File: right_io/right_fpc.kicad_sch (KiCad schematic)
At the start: 1 part

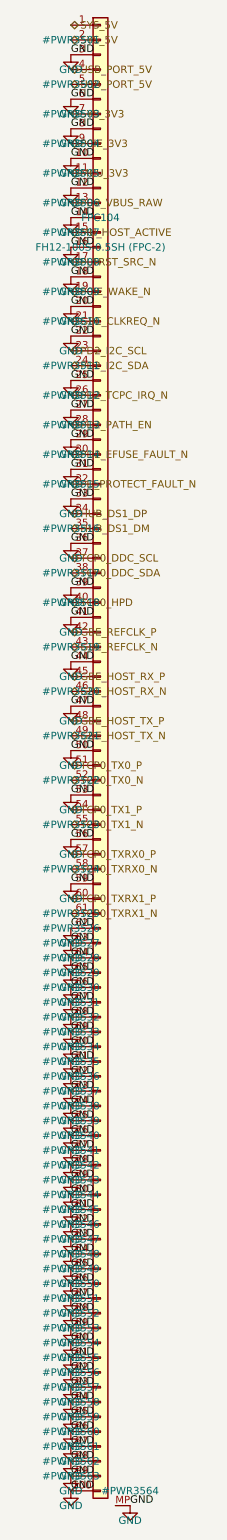
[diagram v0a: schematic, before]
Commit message: Phase 4 deep audit: FH41-68S connectors, placement hygiene, one-shot fixes
Found and fixed four board-killers in the pre-fab audit:

1. Fictional connector: the Hirose FH12 series stops at 60 positions, so
   the 100-pin FH12-100S used for FPC-1/FPC-2 does not exist.  Replaced
   with the FH41-68S-0.5SH(05) (shielded-FFC, 68 positions; FPC-1 uses
   pins 1-53, FPC-2 pins 1-61):
   - new footprint derived from KiCad's FH41-30S (68 signal pads, MP at
     +/-18, 14 SH solder-holds, 38mm body) with SH pads tied to GND
   - new 68-pin symbol (Conn_01x68_FFC_MP), pin maps trimmed to 68
   - fictional FH12-100S footprint/symbol/script removed
   - cable spec updated (68-pin shielded FFC, one type for both)

2. Connector courtyard conflicts: parts sat under connector bodies
   (pads cleared, bodies collided).  Placement now enforces courtyard
   clearance against the connector body; the resolver scans with
   courtyard checks; a double-shift bug that hid re-placed parts' true
   positions was fixed.

3. FPC-3 orientation: the FH12's FPC enters from the +y side; both FPC-3
   connectors faced away from the seam.  FPC105 -> (123.5, 6.5) rot 180,
   FPC106 -> (30, 54) rot 0 so the cable exits the center bottom edge
   and enters the BMS top edge.

4. Original-layout defects: 16 genuine pad-pad shorts (inductor pads
   swallowing caps, passives on each other, parts on mounting holes) and
   23 parts inside the hinge cutouts (physically off the board) are all
   moved to legal spots; zones refilled against the final placement.

New post-build hygiene sweep (fix_board_hygiene.py) uses the final board
text as the geometry oracle, converges to a clean state, and reports
residuals instead of dropping them.

Final DRC: 0 shorts / 0 clearance / 0 hole violations on all four boards
(bms fully clean).  Remaining: courtyard touches around the Mu socket and
M.2 slot (design-inherent moat), chassis-edge copper, zone islands, silk
cosmetics, and unrouted nets (Phase 4b).  Gate: SCHEMATIC R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
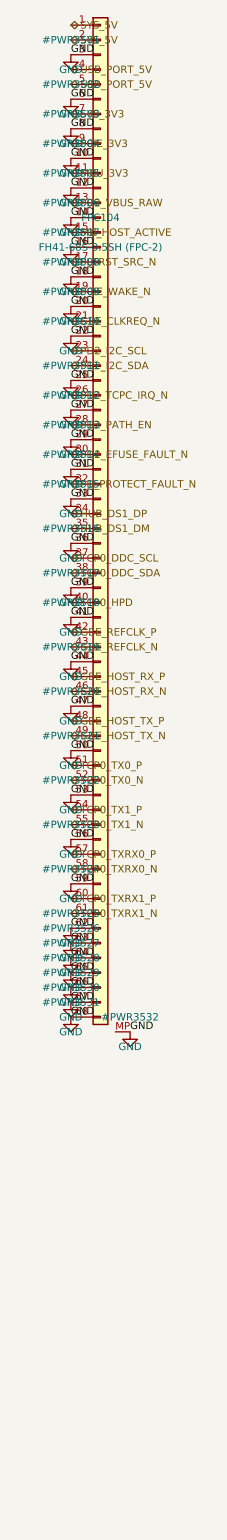
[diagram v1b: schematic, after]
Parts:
- FPC104: value FH12-100S-0.5SH (FPC-2) -> FH41-68S-0.5SH (FPC-2); footprint ducktop2:FH12-100S-0.5SH_1x100-1MP_P0.50mm_Horizontal -> ducktop2:Hirose_FH41-68S-0.5SH_1x68_1MP_1SH_P0.5mm_Horizontal; symbol Conn_01x100_FFC_MP:Conn_01x100_FFC_MP -> Conn_01x68_FFC_MP:Conn_01x68_FFC_MP
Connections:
- net GND: no longer FPC104.100 (Pin_100), FPC104.69 (Pin_69), FPC104.70 (Pin_70), FPC104.71 (Pin_71), FPC104.72 (Pin_72), FPC104.73 (Pin_73), FPC104.74 (Pin_74), FPC104.75 (Pin_75), FPC104.76 (Pin_76), FPC104.77 (Pin_77), FPC104.78 (Pin_78), FPC104.79 (Pin_79), FPC104.80 (Pin_80), FPC104.81 (Pin_81), FPC104.82 (Pin_82), FPC104.83 (Pin_83), FPC104.84 (Pin_84), FPC104.85 (Pin_85), FPC104.86 (Pin_86), FPC104.87 (Pin_87), FPC104.88 (Pin_88), FPC104.89 (Pin_89), FPC104.90 (Pin_90), FPC104.91 (Pin_91), FPC104.92 (Pin_92), FPC104.93 (Pin_93), FPC104.94 (Pin_94), FPC104.95 (Pin_95), FPC104.96 (Pin_96), FPC104.97 (Pin_97), FPC104.98 (Pin_98), FPC104.99 (Pin_99)

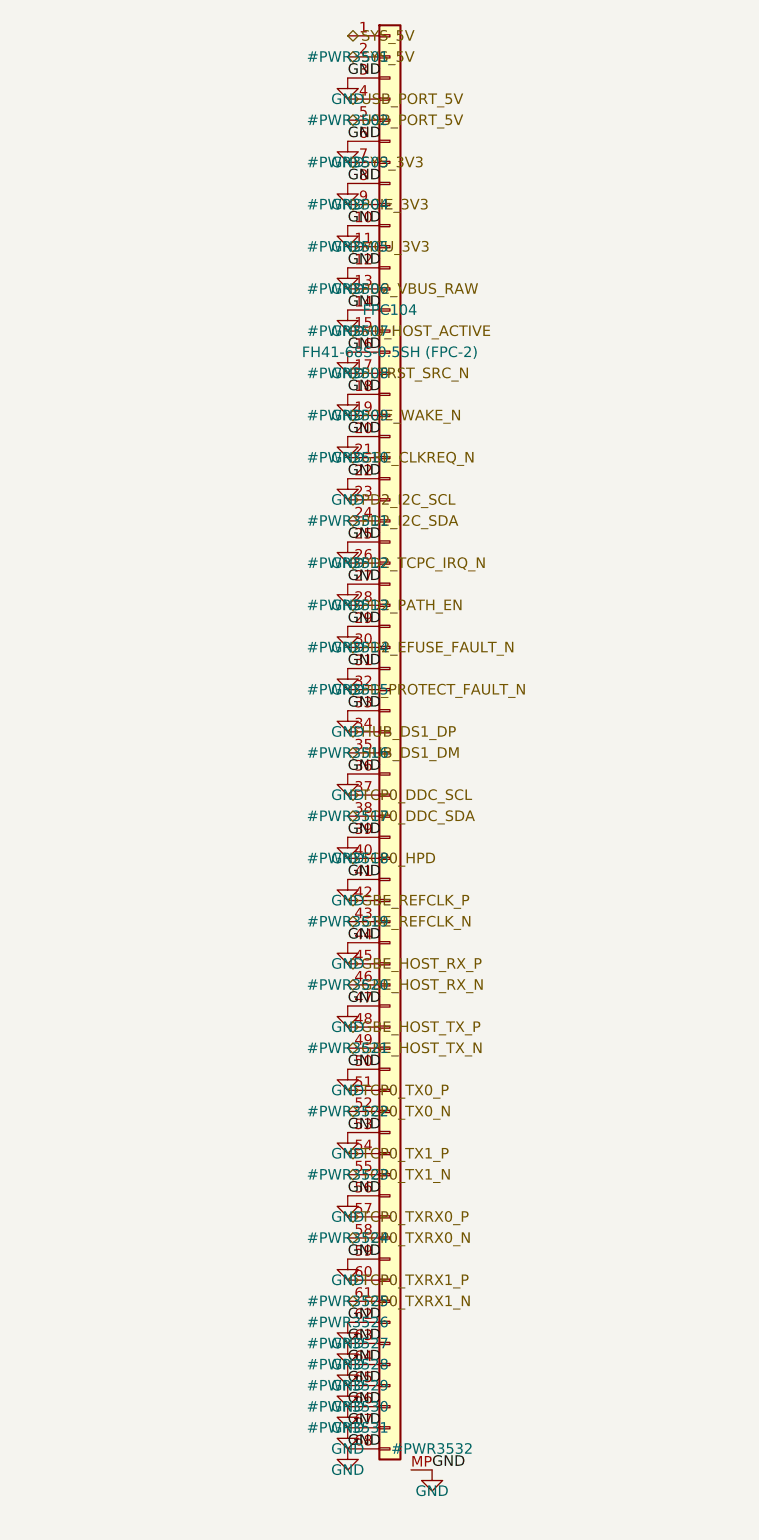
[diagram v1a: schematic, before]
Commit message: Phase 5: second-opinion audit remediation + rebuilt, verified board pipeline
Second-opinion AI audit found A-tier defects; remediation applied and the
board pipeline rebuilt on a known-good base with the fixes it needed:

- electrical: LTC4418IUF symbol pinout corrected (both selectors were
  dead as drawn); center charge cascade (U15 <- U15B, PD1 > PD2 > AUX);
  pack negative never crosses FPC-3, 15-pin FG_VSS return; power-budgeted
  FPC pin maps (0.4 A/pin derate); J12/DS4 completed; AUX source fuse
- FH41-68S footprint: 13 datasheet-correct SH pads + SH pin in symbol
- connector geometry settled against the Hirose FH12 2D drawing: FFC
  enters opposite the solder pins (mouth = local +Y); reversed side-B
  maps are correct for the 180-deg-mounted pairs; rotations set so mouths
  face across every seam
- pipeline (generate_split_boards.py): per-pin pad-net resync from the
  netlists (kills shadow nets for good), netlist-exact name
  normalization, netlist-only part injection (cascade, probe headers),
  zone refill after outline swap, read-before-write race fixed, orphan
  parts dropped loudly, non-zero exit on unresolved overlaps
- monolith board relocated to old/monolith_ducktop2.kicad_pcb (placement
  oracle for the center cut only)

verified end state: 4 boards 0 shorts / 0 clearance / 0 drill, 0 boundary
crossings, 6/6 connectors contract-exact with mouths facing, 0 shadow
nets, gates PASS x4, ERC 0 x4. routing next (499 nets/board).
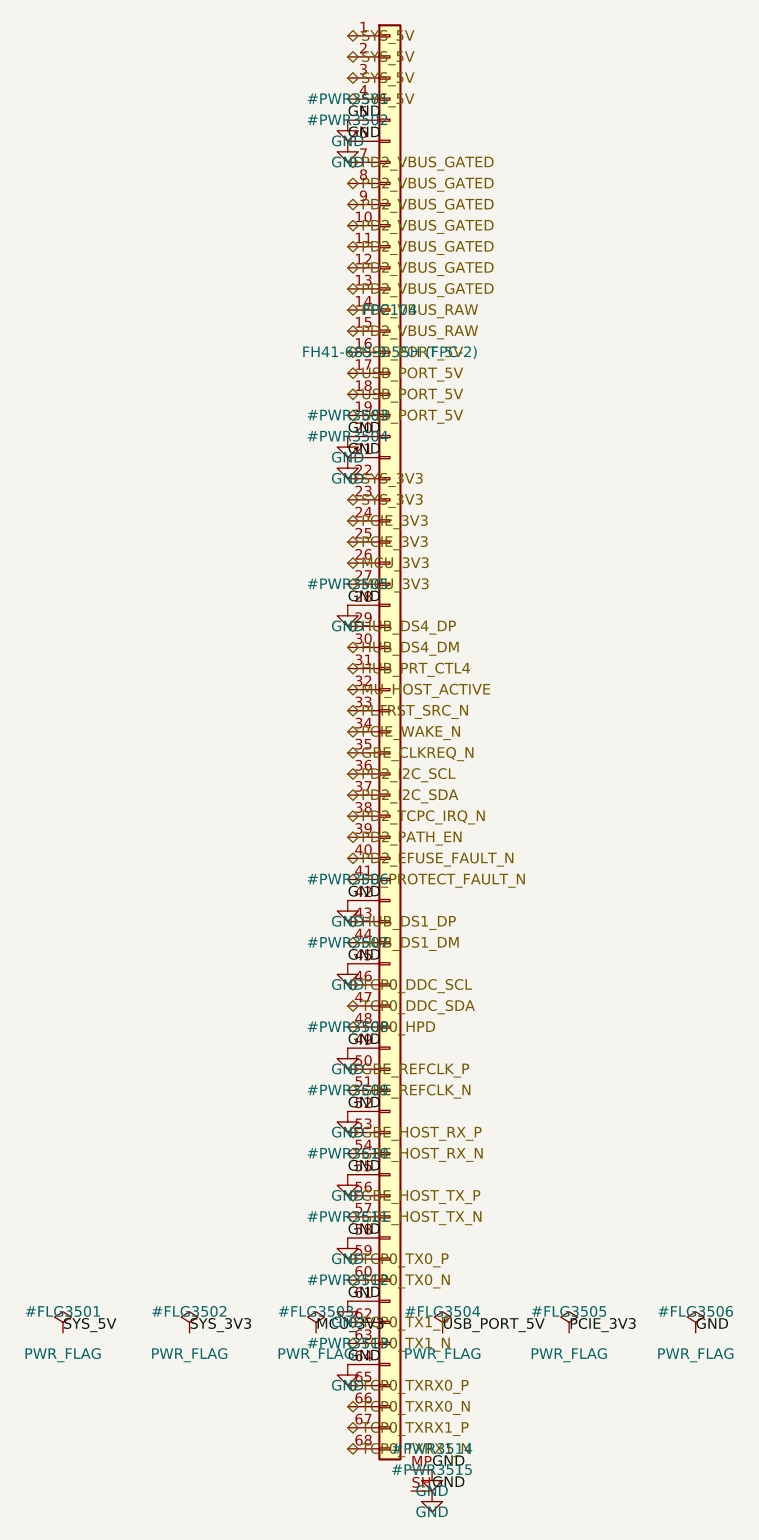
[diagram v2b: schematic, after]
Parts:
- FPC104: MPN (none) -> FH41-68S-0.5SH(05); Manufacturer (none) -> Hirose
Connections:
- net GBE_CLKREQ_N: now also FPC104.35 (Pin_35); no longer FPC104.21 (Pin_21)
- net GBE_HOST_RX_N: now also FPC104.54 (Pin_54); no longer FPC104.46 (Pin_46)
- net GBE_HOST_RX_P: now also FPC104.53 (Pin_53); no longer FPC104.45 (Pin_45)
- net GBE_HOST_TX_N: now also FPC104.57 (Pin_57); no longer FPC104.49 (Pin_49)
- net GBE_HOST_TX_P: now also FPC104.56 (Pin_56); no longer FPC104.48 (Pin_48)
- net GBE_REFCLK_N: now also FPC104.51 (Pin_51); no longer FPC104.43 (Pin_43)
- net GBE_REFCLK_P: now also FPC104.50 (Pin_50); no longer FPC104.42 (Pin_42)
- net GND: now also FPC104.21 (Pin_21), FPC104.28 (Pin_28), FPC104.42 (Pin_42), FPC104.45 (Pin_45), FPC104.49 (Pin_49), FPC104.5 (Pin_5), FPC104.52 (Pin_52), FPC104.55 (Pin_55), FPC104.58 (Pin_58), FPC104.61 (Pin_61), FPC104.SH; no longer FPC104.10 (Pin_10), FPC104.12 (Pin_12), FPC104.14 (Pin_14), FPC104.16 (Pin_16), FPC104.18 (Pin_18), FPC104.22 (Pin_22), FPC104.25 (Pin_25), FPC104.27 (Pin_27), FPC104.29 (Pin_29), FPC104.3 (Pin_3), FPC104.31 (Pin_31), FPC104.33 (Pin_33), FPC104.36 (Pin_36), FPC104.39 (Pin_39), FPC104.41 (Pin_41), FPC104.44 (Pin_44), FPC104.47 (Pin_47), FPC104.50 (Pin_50), FPC104.53 (Pin_53), FPC104.56 (Pin_56), FPC104.59 (Pin_59), FPC104.62 (Pin_62), FPC104.63 (Pin_63), FPC104.65 (Pin_65), FPC104.66 (Pin_66), FPC104.67 (Pin_67), FPC104.68 (Pin_68), FPC104.8 (Pin_8)
- net HUB_DS1_DM: now also FPC104.44 (Pin_44); no longer FPC104.35 (Pin_35)
- net HUB_DS1_DP: now also FPC104.43 (Pin_43); no longer FPC104.34 (Pin_34)
- net MCU_3V3: now also FPC104.26 (Pin_26), FPC104.27 (Pin_27); no longer FPC104.11 (Pin_11)
- net MU_HOST_ACTIVE: now also FPC104.32 (Pin_32); no longer FPC104.15 (Pin_15)
- net PCIE_3V3: now also FPC104.24 (Pin_24), FPC104.25 (Pin_25); no longer FPC104.9 (Pin_9)
- net PCIE_WAKE_N: now also FPC104.34 (Pin_34); no longer FPC104.19 (Pin_19)
- net PD2_EFUSE_FAULT_N: now also FPC104.40 (Pin_40); no longer FPC104.30 (Pin_30)
- net PD2_I2C_SCL: now also FPC104.36 (Pin_36); no longer FPC104.23 (Pin_23)
- net PD2_I2C_SDA: now also FPC104.37 (Pin_37); no longer FPC104.24 (Pin_24)
- net PD2_PATH_EN: now also FPC104.39 (Pin_39); no longer FPC104.28 (Pin_28)
- net PD2_TCPC_IRQ_N: now also FPC104.38 (Pin_38); no longer FPC104.26 (Pin_26)
- net PD2_VBUS_RAW: now also FPC104.14 (Pin_14), FPC104.15 (Pin_15); no longer FPC104.13 (Pin_13)
- net PD_PROTECT_FAULT_N: now also FPC104.41 (Pin_41); no longer FPC104.32 (Pin_32)
- net PLTRST_SRC_N: now also FPC104.33 (Pin_33); no longer FPC104.17 (Pin_17)
- net SYS_3V3: now also FPC104.22 (Pin_22), FPC104.23 (Pin_23); no longer FPC104.7 (Pin_7)
- net SYS_5V: now also FPC104.3 (Pin_3), FPC104.4 (Pin_4)
- net TCP0_DDC_SCL: now also FPC104.46 (Pin_46); no longer FPC104.37 (Pin_37)
- net TCP0_DDC_SDA: now also FPC104.47 (Pin_47); no longer FPC104.38 (Pin_38)
- net TCP0_HPD: now also FPC104.48 (Pin_48); no longer FPC104.40 (Pin_40)
- net TCP0_TX0_N: now also FPC104.60 (Pin_60); no longer FPC104.52 (Pin_52)
- net TCP0_TX0_P: now also FPC104.59 (Pin_59); no longer FPC104.51 (Pin_51)
- net TCP0_TX1_N: now also FPC104.63 (Pin_63); no longer FPC104.55 (Pin_55)
- net TCP0_TX1_P: now also FPC104.62 (Pin_62); no longer FPC104.54 (Pin_54)
- net TCP0_TXRX0_N: now also FPC104.66 (Pin_66); no longer FPC104.58 (Pin_58)
- net TCP0_TXRX0_P: now also FPC104.65 (Pin_65); no longer FPC104.57 (Pin_57)
- net TCP0_TXRX1_N: now also FPC104.68 (Pin_68); no longer FPC104.61 (Pin_61)
- net TCP0_TXRX1_P: now also FPC104.67 (Pin_67); no longer FPC104.60 (Pin_60)
- net USB_PORT_5V: now also FPC104.16 (Pin_16), FPC104.17 (Pin_17), FPC104.18 (Pin_18), FPC104.19 (Pin_19); no longer FPC104.4 (Pin_4), FPC104.5 (Pin_5)
- new net HUB_DS4_DM: FPC104.30 (Pin_30)
- new net HUB_DS4_DP: FPC104.29 (Pin_29)
- new net HUB_PRT_CTL4: FPC104.31 (Pin_31)
- new net PD2_VBUS_GATED: FPC104.10 (Pin_10), FPC104.11 (Pin_11), FPC104.12 (Pin_12), FPC104.13 (Pin_13), FPC104.7 (Pin_7), FPC104.8 (Pin_8), FPC104.9 (Pin_9)

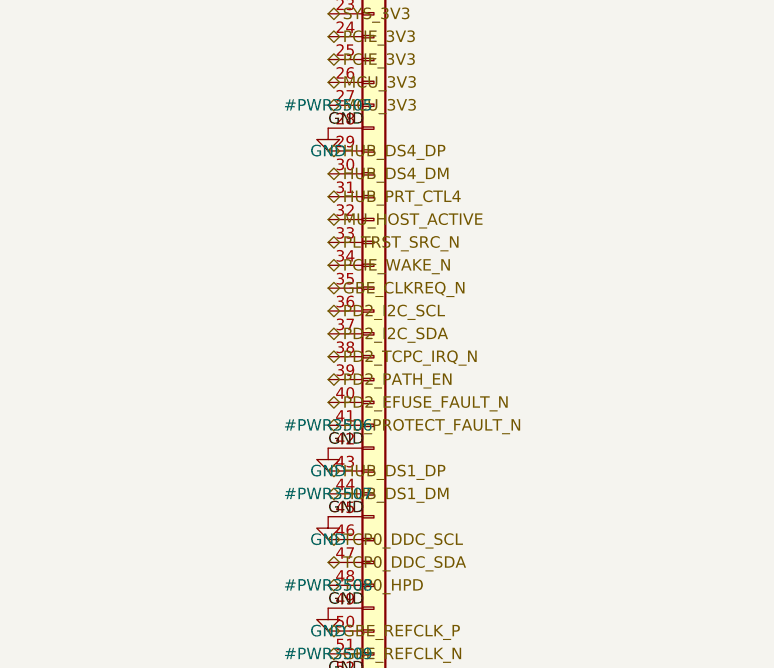
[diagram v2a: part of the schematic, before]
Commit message: get the main boards ready for routing
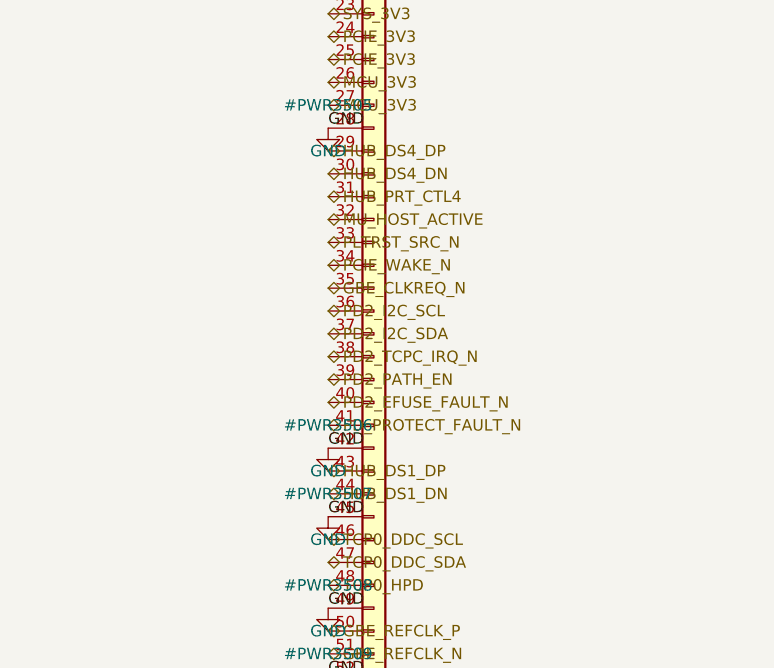
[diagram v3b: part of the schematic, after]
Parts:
- FPC104: MPN FH41-68S-0.5SH(05) -> FH41-68S-0.5SH(28)
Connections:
- net HUB_DS1_DM renamed HUB_DS1_DN
- net HUB_DS4_DM renamed HUB_DS4_DN
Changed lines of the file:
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@@
   (property "Datasheet" "" (at 59.69 299.72 0) (effects (font (size 1.27 1.27)) (hide yes)))
   (property "Manufacturer" "Hirose" (at 59.69 299.72 0) (effects (font (size 1.27 1.27)) (hide yes)))
-  (property "MPN" "FH41-68S-0.5SH(05)" (at 59.69 299.72 0) (effects (font (size 1.27 1.27)) (hide yes)))
+  (property "MPN" "FH41-68S-0.5SH(28)" (at 59.69 299.72 0) (effects (font (size 1.27 1.27)) (hide yes)))
   (pin "1")
   (pin "2")
@@
   (effects (font (size 1.27 1.27)) (justify left bottom))
 )
-(hierarchical_label "HUB_DS4_DM"
+(hierarchical_label "HUB_DS4_DN"
   (shape bidirectional)
   (at 54.61 337.82 0)
@@
   (effects (font (size 1.27 1.27)) (justify left bottom))
 )
-(hierarchical_label "HUB_DS1_DM"
+(hierarchical_label "HUB_DS1_DN"
   (shape bidirectional)
   (at 54.61 373.38 0)

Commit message: fix the center layout and more board issues
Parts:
- added J2433: right power loom, straight-numbered, Connector_Molex:Molex_Micro-Fit_3.0_43045-1012_2x05_P3.00mm_Vertical, symbol Connector_Generic:Conn_02x05_Odd_Even
- added J2435: USB5 direct power loom, ducktop2:AMASS_XT30PW-F30_G_Y, symbol Connector_Generic:Conn_01x02
- added J2445, J2447: main ground strap, Connector_Wire:SolderWirePad_1x01_SMD_5x10mm, symbol Connector:TestPoint
- added R2446, R2447: 0.33, Resistor_SMD:R_0603_1608Metric, symbol Device:R
- FPC104: value FH41-68S-0.5SH (FPC-2) -> Molex5039085120 signal cable; footprint ducktop2:Hirose_FH41-68S-0.5SH_1x68_1MP_1SH_P0.5mm_Horizontal -> ducktop2:Molex_5039085120_1x51_P0.50mm_Horizontal; symbol Conn_01x68_FFC_MP:Conn_01x68_FFC_MP -> Conn_01x51_Signal_SH:Conn_01x51_Signal_SH; MPN FH41-68S-0.5SH(28) -> 5039085120; Manufacturer Hirose -> Molex
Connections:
- net GBE_CLKREQ_N: now also FPC104.50; no longer FPC104.35 (Pin_35)
- net GBE_HOST_RX_N: now also FPC104.15; no longer FPC104.54 (Pin_54)
- net GBE_HOST_RX_P: now also FPC104.14; no longer FPC104.53 (Pin_53)
- net GBE_HOST_TX_N: now also FPC104.18; no longer FPC104.57 (Pin_57)
- net GBE_HOST_TX_P: now also FPC104.17; no longer FPC104.56 (Pin_56)
- net GBE_REFCLK_N: now also FPC104.21; no longer FPC104.51 (Pin_51)
- net GBE_REFCLK_P: now also FPC104.20; no longer FPC104.50 (Pin_50)
- net GND: now also FPC104.1, FPC104.10, FPC104.13, FPC104.16, FPC104.19, FPC104.22, FPC104.25, FPC104.32, FPC104.36, FPC104.4, FPC104.40, FPC104.44, FPC104.48, FPC104.51, FPC104.7, J2433.10 (Pin_10), J2433.7 (Pin_7), J2433.8 (Pin_8), J2433.9 (Pin_9), J2435.1 (Pin_1), J2445.1, J2447.1, R2446.2, R2447.2; no longer FPC104.20 (Pin_20), FPC104.21 (Pin_21), FPC104.42 (Pin_42), FPC104.45 (Pin_45), FPC104.49 (Pin_49), FPC104.5 (Pin_5), FPC104.52 (Pin_52), FPC104.55 (Pin_55), FPC104.58 (Pin_58), FPC104.6 (Pin_6), FPC104.61 (Pin_61), FPC104.64 (Pin_64), FPC104.MP, FPC104.SH
- net HUB_DS1_DN: now also FPC104.24; no longer FPC104.44 (Pin_44)
- net HUB_DS1_DP: now also FPC104.23; no longer FPC104.43 (Pin_43)
- net HUB_DS4_DN: now also FPC104.27; no longer FPC104.30 (Pin_30)
- net HUB_DS4_DP: now also FPC104.26; no longer FPC104.29 (Pin_29)
- net HUB_PRT_CTL4: now also FPC104.45; no longer FPC104.31 (Pin_31)
- net MCU_3V3: now also J2433.6 (Pin_6); no longer FPC104.26 (Pin_26), FPC104.27 (Pin_27)
- net MU_HOST_ACTIVE: now also FPC104.46; no longer FPC104.32 (Pin_32)
- net PCIE_3V3: now also J2433.5 (Pin_5); no longer FPC104.24 (Pin_24), FPC104.25 (Pin_25)
- net PCIE_WAKE_N: now also FPC104.49; no longer FPC104.34 (Pin_34)
- net PD2_EFUSE_FAULT_N: now also FPC104.38; no longer FPC104.40 (Pin_40)
- net PD2_I2C_SCL: now also FPC104.33; no longer FPC104.36 (Pin_36)
- net PD2_I2C_SDA: now also FPC104.34; no longer FPC104.37 (Pin_37)
- net PD2_PATH_EN: now also FPC104.37; no longer FPC104.39 (Pin_39)
- net PD2_TCPC_IRQ_N: now also FPC104.35; no longer FPC104.38 (Pin_38)
- net PD2_VBUS_GATED: now also J2433.1 (Pin_1); no longer FPC104.10 (Pin_10), FPC104.11 (Pin_11), FPC104.12 (Pin_12), FPC104.13 (Pin_13), FPC104.7 (Pin_7), FPC104.8 (Pin_8), FPC104.9 (Pin_9)
- net PD2_VBUS_RAW: now also J2433.2 (Pin_2); no longer FPC104.14 (Pin_14), FPC104.15 (Pin_15)
- net PD_PROTECT_FAULT_N: now also FPC104.39; no longer FPC104.41 (Pin_41)
- net PLTRST_SRC_N: now also FPC104.47; no longer FPC104.33 (Pin_33)
- net SYS_3V3: now also J2433.4 (Pin_4); no longer FPC104.22 (Pin_22), FPC104.23 (Pin_23)
- net SYS_5V: now also J2433.3 (Pin_3); no longer FPC104.1 (Pin_1), FPC104.2 (Pin_2), FPC104.3 (Pin_3), FPC104.4 (Pin_4)
- net TCP0_DDC_SCL: now also FPC104.29; no longer FPC104.46 (Pin_46)
- net TCP0_DDC_SDA: now also FPC104.30; no longer FPC104.47 (Pin_47)
- net TCP0_HPD: now also FPC104.31; no longer FPC104.48 (Pin_48)
- net TCP0_TX0_N: now also FPC104.3; no longer FPC104.60 (Pin_60)
- net TCP0_TX0_P: now also FPC104.2; no longer FPC104.59 (Pin_59)
- net TCP0_TX1_N: now also FPC104.6; no longer FPC104.63 (Pin_63)
- net TCP0_TX1_P: now also FPC104.5; no longer FPC104.62 (Pin_62)
- net TCP0_TXRX0_N: now also FPC104.9; no longer FPC104.66 (Pin_66)
- net TCP0_TXRX0_P: now also FPC104.8; no longer FPC104.65 (Pin_65)
- net TCP0_TXRX1_N: now also FPC104.12; no longer FPC104.68 (Pin_68)
- net TCP0_TXRX1_P: now also FPC104.11; no longer FPC104.67 (Pin_67)
- net USB_PORT_5V: now also J2435.2 (Pin_2); no longer FPC104.16 (Pin_16), FPC104.17 (Pin_17), FPC104.18 (Pin_18), FPC104.19 (Pin_19)
- new net FPC104_SHELL: FPC104.SH, R2446.1, R2447.1
- new net PD2_SOURCE_PG: FPC104.41
- new net USB_J11_PERMIT: FPC104.42
- new net USB_J12_PERMIT: FPC104.43
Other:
- note added: "Both ground straps must be fitted before the signal cable. Keep raw and protected battery returns separate from these main-board grounds."
- note added: "Power uses the separate rated looms. The signal cable carries no positive supply rails."
- note added: "The shell uses two parallel 0.33 ohm returns at each connector. Numbered ground conductors connect directly to the local ground plane."
